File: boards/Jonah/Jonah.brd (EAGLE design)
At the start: 54.6 x 25.4 mm, 10 parts

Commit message: First pass at Jonah board v2
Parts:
- removed XBEE: XBEE-1B2, SparkFun-RF:XBEE-SILK
- added RF_TX: 434 MHz, SparkFun-Connectors:1X04
- moved R_T0 19.6 mm to (2.54, 6.99), turned to 90 degrees
- moved R2 8.64 mm to (13.3, 12.1)
- moved R1 8.64 mm to (13.3, 8.26)
- moved MAIN 8.52 mm to (12.7, 8.89)
- moved THERM0 7.65 mm to (2.54, 10.8)
- moved ARDUINO 4.58 mm to (24.1, 8.89)
- moved R_SCL 4.58 mm to (29.2, 7.62)
- moved R_SDA 4.58 mm to (26.7, 7.62)
- moved BMP085 4.02 mm to (6.35, 15.2)
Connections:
- removed net N$3: ARDUINO.TXO, XBEE.3
- removed net N$4: ARDUINO.RXI, XBEE.2
- net 3.3V: now also RF_TX.3; no longer XBEE.1
- net GND: now also RF_TX.1; no longer XBEE.10
- net N$1: now also ARDUINO.TXO, RF_TX.2; no longer ARDUINO.RST0, XBEE.5
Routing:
- net N$4: track 24.5 -> 0.00 mm
- net N$3: track 19.4 -> 0.00 mm
- net N$2: track 34.5 -> 19.9 mm
- net A0: track 17.7 -> 28.1 mm
- net N$1: track 21.0 -> 11.0 mm
- net 3.3V: track 53.3 -> 43.8 mm
- net GND: track 63.7 -> 55.5 mm
- net SDA: track 25.0 -> 23.7 mm
- net SCL: track 28.3 -> 27.5 mm
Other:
- board size 54.6 x 25.4 mm -> 50.8 x 17.8 mm
- board text added: "Jonah v2"
- board text removed: "Jonah v1"

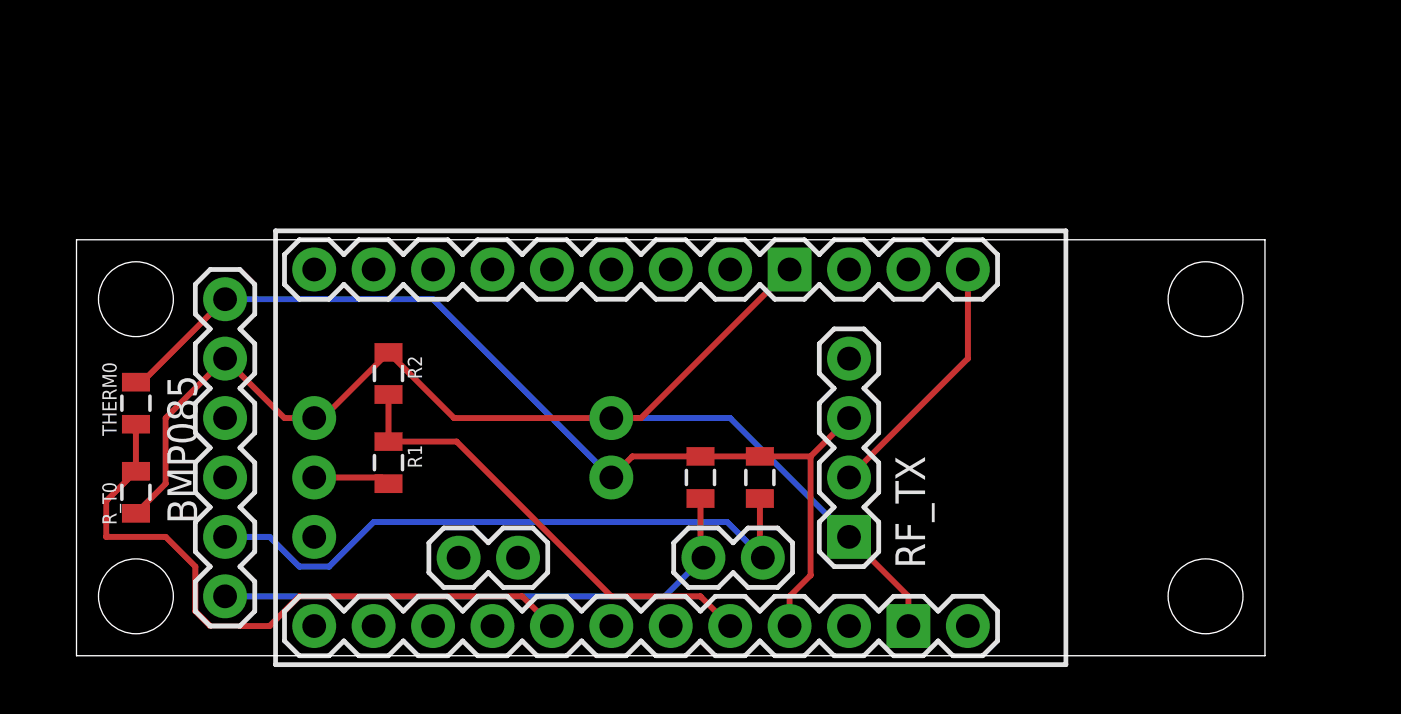
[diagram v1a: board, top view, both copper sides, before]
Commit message: Jonah board v2
Rearranged things, and now use SparkFun's KLP radio, not an Xbee.

Also, made some space and holes for attaching to a rod.
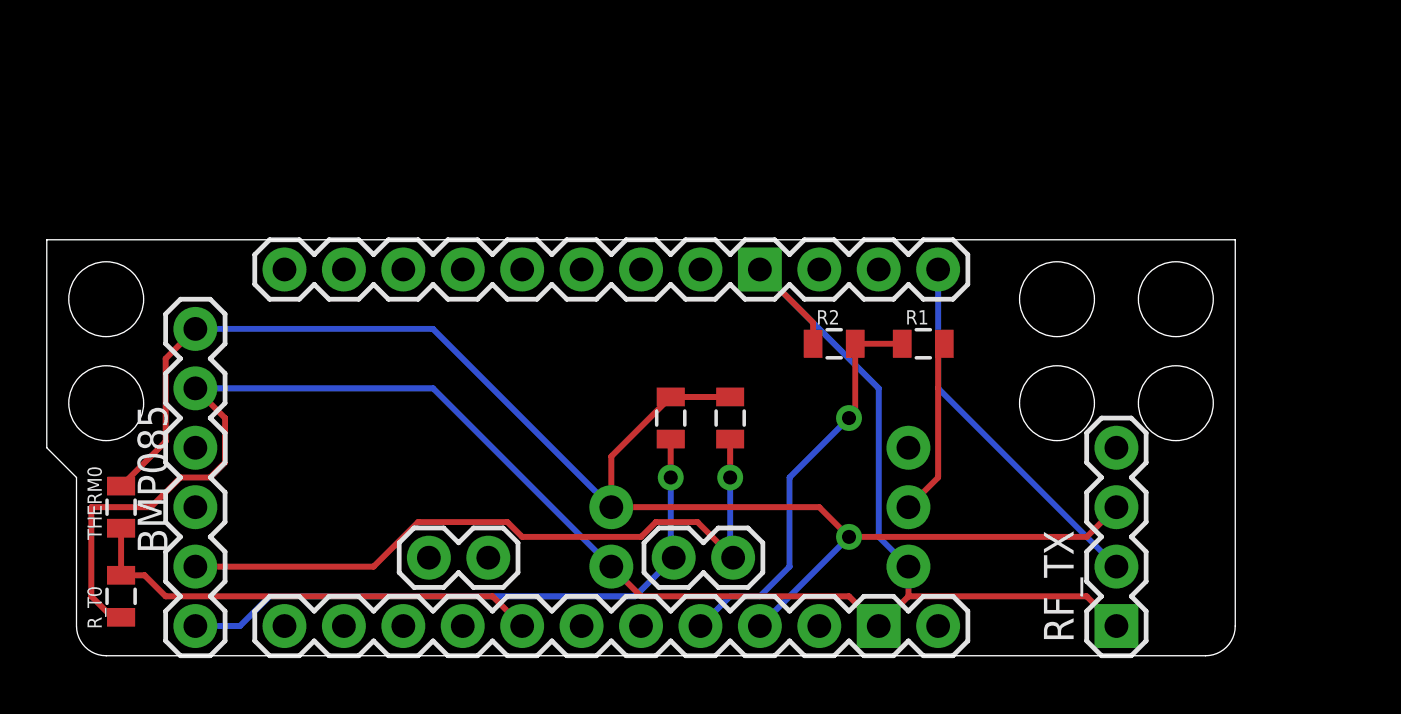
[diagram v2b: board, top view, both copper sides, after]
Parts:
- ARDUINO: value ARDUINO_PRO_MINI -> ARDUINO_PRO_MINI-NOSILK; device OpenSpace:ARDUINO_PRO_MINI -> OpenSpace:ARDUINO_PRO_MINI-NOSILK
- moved R1 23.4 mm to (36.2, 13.3), turned to 0 degrees
- moved MAIN 20.7 mm to (33.0, 5.08), turned to 0 degrees
- moved R2 19.1 mm to (32.4, 13.3), turned to 0 degrees
- moved RF_TX 12.0 mm to (44.5, 1.27)
- moved R_T0 4.49 mm to (1.91, 2.54)
- moved THERM0 4.49 mm to (1.91, 6.35)
- moved R_SDA 2.84 mm to (25.4, 10.2)
- moved R_SCL 2.84 mm to (27.9, 10.2)
- moved BMP085 1.80 mm to (5.08, 14.0)
- moved ARDUINO 1.27 mm to (22.9, 8.89)
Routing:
- net GND: track 55.5 -> 81.0 mm
- net 3.3V: track 43.8 -> 65.3 mm, vias 0 -> 1
- net A0: track 28.1 -> 20.1 mm
- net N$1: track 11.0 -> 15.9 mm
- net 1.8V: track 3.28 -> 7.62 mm
- net SDA: track 23.7 -> 26.8 mm, vias 0 -> 1
- net SCL: track 27.5 -> 30.1 mm, vias 0 -> 1
- net N$2: track 19.9 -> 17.6 mm, vias 0 -> 1
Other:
- outline, holes or cut-outs redrawn
